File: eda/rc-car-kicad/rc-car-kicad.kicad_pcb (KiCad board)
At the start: 2 copper layers, 81.5 x 40 mm, 55 parts, among them Q1 MMBT3904, Q2 IRLML2246, Q3 IRLML2246, Q4 MMBT3904, Q5 IRLML6244, Q6 IRLML6244, SW1 SW_SPST, U1 TPS3840, U2 MIC3975-5.0YMM, U3 MIC5225-3.3YM5, U4 ATmega164A-A

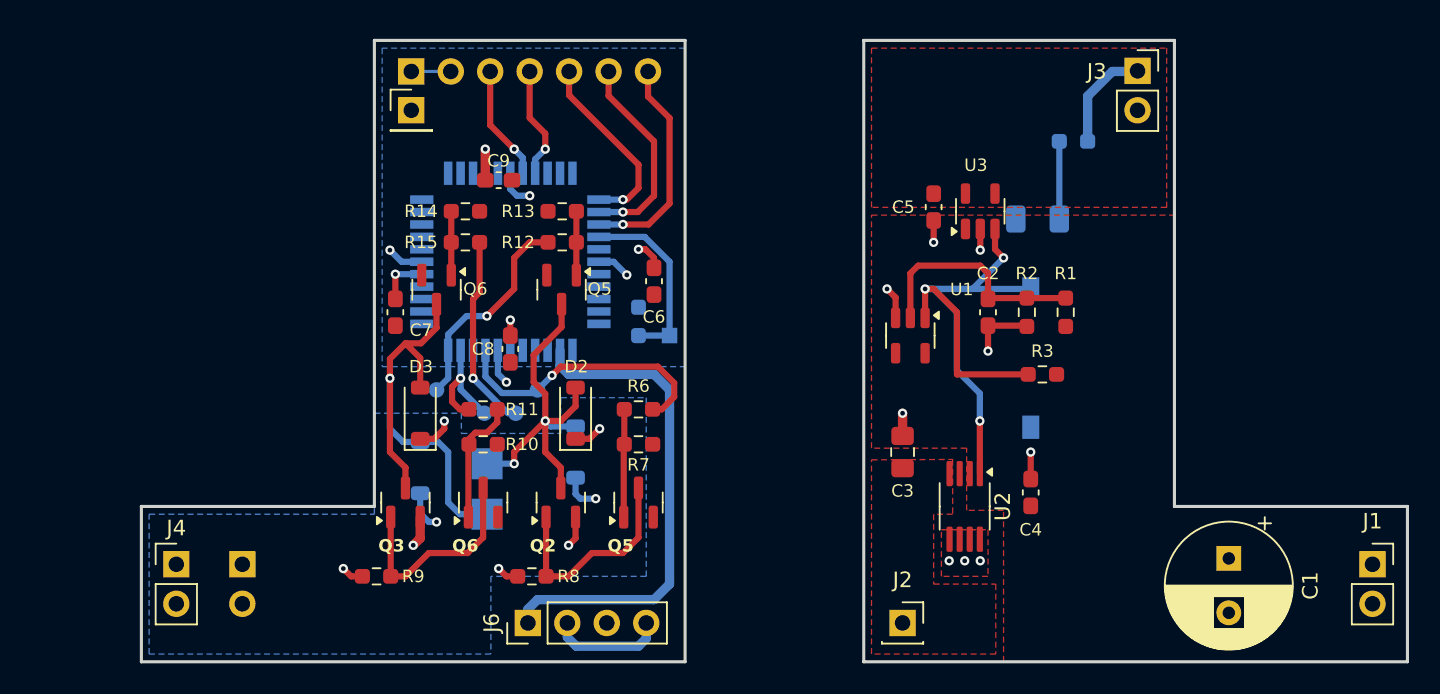
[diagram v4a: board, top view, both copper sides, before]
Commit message: - Modified the header pins a bit on the pcb
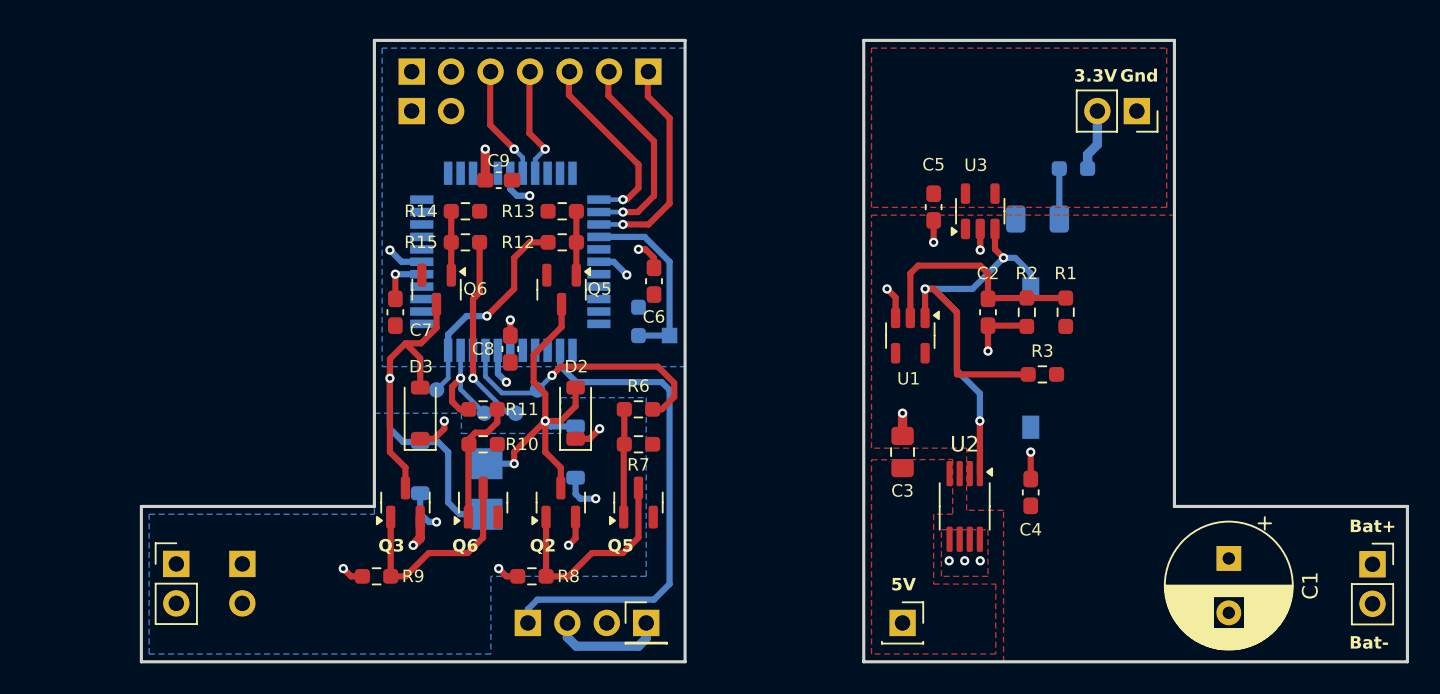
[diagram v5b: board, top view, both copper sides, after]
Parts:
- added J16: ~, _global-libraries:PinHeader_1x02_P2.54mm_Vertical_No_Courtyard, F.Cu at (124.4, 105.0)
- added J17: ~, Connector_PinHeader_2.54mm:PinHeader_1x01_P2.54mm_Vertical, F.Cu at (139.5, 138.0)
- J6: footprint Connector_PinHeader_2.54mm:PinHeader_1x04_P2.54mm_Vertical -> Connector_PinHeader_2.54mm:PinHeader_1x03_P2.54mm_Vertical; moved to B.Cu
- J7: footprint Connector_PinHeader_2.54mm:PinHeader_1x01_P2.54mm_Vertical -> _global-libraries:PinHeader_1x02_P2.54mm_Vertical_No_Courtyard; moved to B.Cu
- J8: footprint Connector_PinHeader_2.54mm:PinHeader_1x07_P2.54mm_Vertical -> Connector_PinHeader_2.54mm:PinHeader_1x05_P2.54mm_Vertical
- moved J8 15.3 mm to (139.6, 102.5), turned to 90 degrees
- moved J3 2.59 mm to (171.1, 105.0), turned to -90 degrees
- moved J7 2.49 mm to (124.4, 102.5), turned to -90 degrees
- moved R4 1.75 mm to (167.0, 108.8)
- turned J6 to -90 degrees
- renumbered Motor- to J10, Motor+ to J9
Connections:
- J3 pad 1: +3.3V Main -> GND Main
- J3 pad 2: GND Main -> +3.3V Main
- J8 pad 1: +3.3V -> /SCK
- J8 pad 2: +3.3V -> /MISO
- J8 pad 3: /CE -> /MOSI
- J8 pad 5: /MOSI -> /CE
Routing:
- net /U1-Reset: track 41.6 -> 37.9 mm
- net +3.3V Main: track 6.78 -> 3.96 mm
- net +3.3V: track 10.7 -> 8.15 mm
- net Net-(D1-A): track 5.00 -> 3.25 mm
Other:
- board text added: "5V"
- board text added: "Bat+"
- board text added: "Bat-"
- board text added: "V+"
- board text added: "V-"

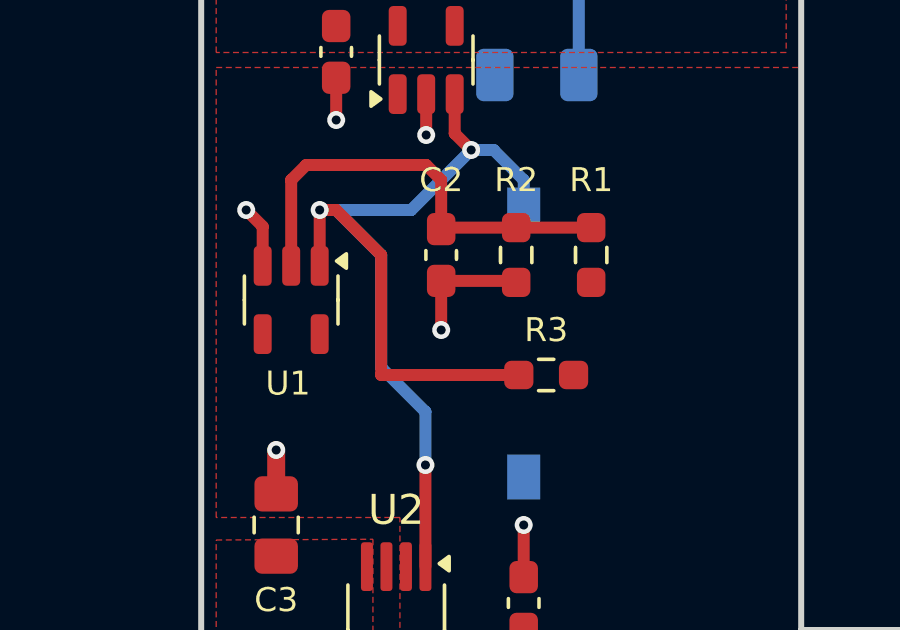
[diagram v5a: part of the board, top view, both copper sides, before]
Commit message: - Updated panelized board. Fixed all design route errors
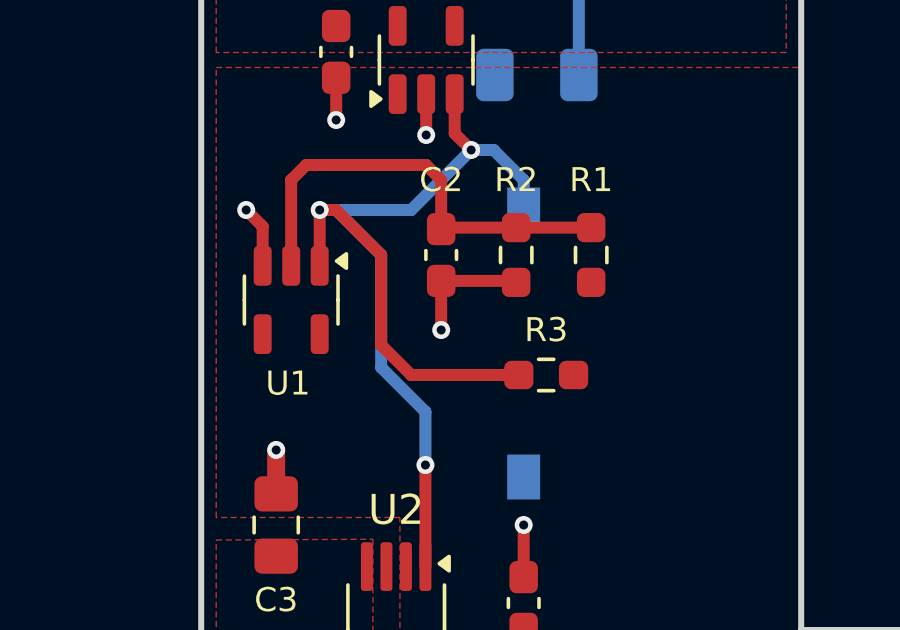
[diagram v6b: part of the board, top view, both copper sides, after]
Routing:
- net /U1-Reset: track 37.9 -> 37.3 mm
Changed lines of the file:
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@@
 	)
 	(setup
+		(stackup
+			(layer "F.SilkS"
+				(type "Top Silk Screen")
+			)
+			(layer "F.Paste"
+				(type "Top Solder Paste")
+			)
+			(layer "F.Mask"
+				(type "Top Solder Mask")
+				(color "Black")
+				(thickness 0.01)
+			)
+			(layer "F.Cu"
+				(type "copper")
+				(thickness 0.035)
+			)
+			(layer "dielectric 1"
+				(type "core")
+				(thickness 1.51)
+				(material "FR4")
+				(epsilon_r 4.5)
+				(loss_tangent 0.02)
+			)
+			(layer "B.Cu"
+				(type "copper")
+				(thickness 0.035)
+			)
+			(layer "B.Mask"
+				(type "Bottom Solder Mask")
+				(color "Black")
+				(thickness 0.01)
+			)
+			(layer "B.Paste"
+				(type "Bottom Solder Paste")
+			)
+			(layer "B.SilkS"
+				(type "Bottom Silk Screen")
+			)
+			(copper_finish "None")
+			(dielectric_constraints no)
+		)
 		(pad_to_mask_clearance 0)
 		(allow_soldermask_bridges_in_footprints no)
@@
 		(tags "Through hole pin header THT 1x02 2.54mm single row")
 		(property "Reference" "J16"
-			(at 0 -2.33 270)
+			(at 0 -2.33 -90)
 			(layer "F.SilkS")
 			(hide yes)
@@
 		)
 		(property "Value" "~"
-			(at 0 4.87 270)
+			(at 0 4.87 -90)
 			(layer "F.Fab")
 			(hide yes)
@@
 		)
 		(fp_text user "${REFERENCE}"
-			(at 0 1.27 360)
+			(at 0 1.27 0)
 			(layer "F.Fab")
 			(effects
@@
 		(tags "Through hole pin header THT 1x05 2.54mm single row")
 		(property "Reference" "J8"
-			(at 0 2.33 270)
+			(at 0 2.33 -90)
 			(layer "B.SilkS")
 			(hide yes)
@@
 		)
 		(property "Value" "~"
-			(at 0 -12.49 270)
+			(at 0 -12.49 -90)
 			(layer "B.Fab")
 			(hide yes)
@@
 		)
 		(fp_text user "${REFERENCE}"
-			(at 0 -5.08 360)
+			(at 0 -5.08 0)
 			(layer "B.Fab")
 			(effects
@@
 	)
 	(segment
-		(start 164.0875 122)
-		(end 159.5 122)
+		(start 160.5 122)
+		(end 159.5 121)
 		(width 0.4)
 		(layer "F.Cu")
@@
 	)
 	(segment
-		(start 159.5 118)
-		(end 158 116.5)
+		(start 161.95 113.95)
+		(end 162.5 114.5)
 		(width 0.4)
 		(layer "F.Cu")
@@
 	)
 	(segment
-		(start 161.95 113.95)
-		(end 162.5 114.5)
+		(start 159.5 121)
+		(end 159.5 118)
 		(width 0.4)
 		(layer "F.Cu")
@@
 	)
 	(segment
-		(start 157.45 116.5)
-		(end 157.45 118.3625)
+		(start 164.0875 122)
+		(end 160.5 122)
 		(width 0.4)
 		(layer "F.Cu")
@@
 	)
 	(segment
-		(start 159.5 122)
-		(end 159.5 118)
+		(start 157.45 116.5)
+		(end 157.45 118.3625)
 		(width 0.4)
 		(layer "F.Cu")
@@
 		(net 30)
 	)
+	(segment
+		(start 159.5 118)
+		(end 158 116.5)
+		(width 0.4)
+		(layer "F.Cu")
+		(net 30)
+	)
 	(via
 		(at 160.975 125)
@@
 		(polygon
 			(pts
-				(xy 154 111.25) (xy 154 107.5) (xy 154 107.5) (xy 154 101) (xy 173 101) (xy 173 111.25)
+				(xy 154 111.25) (xy 154 107.5) (xy 154 101) (xy 173 101) (xy 173 111.25)
 			)
 		)

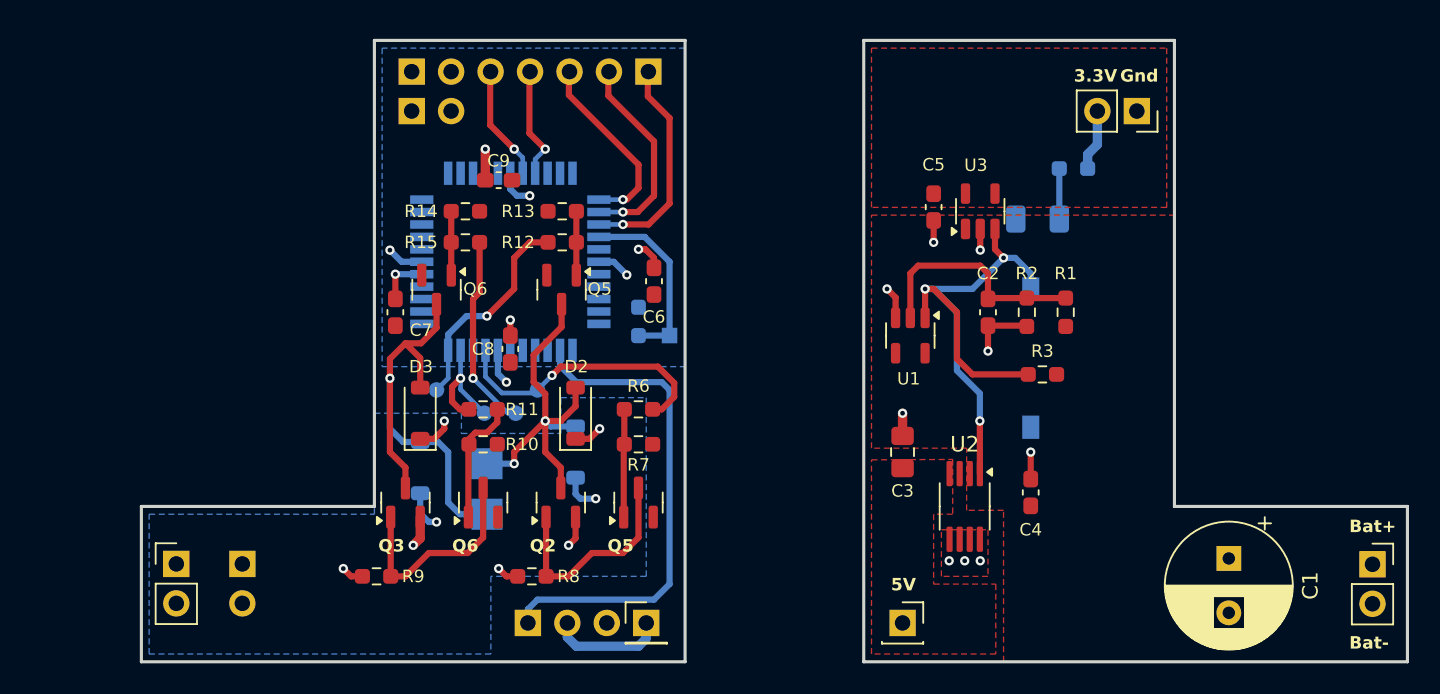
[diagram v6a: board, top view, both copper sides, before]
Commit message: - Documented the schematic and created a pdf of the schematic
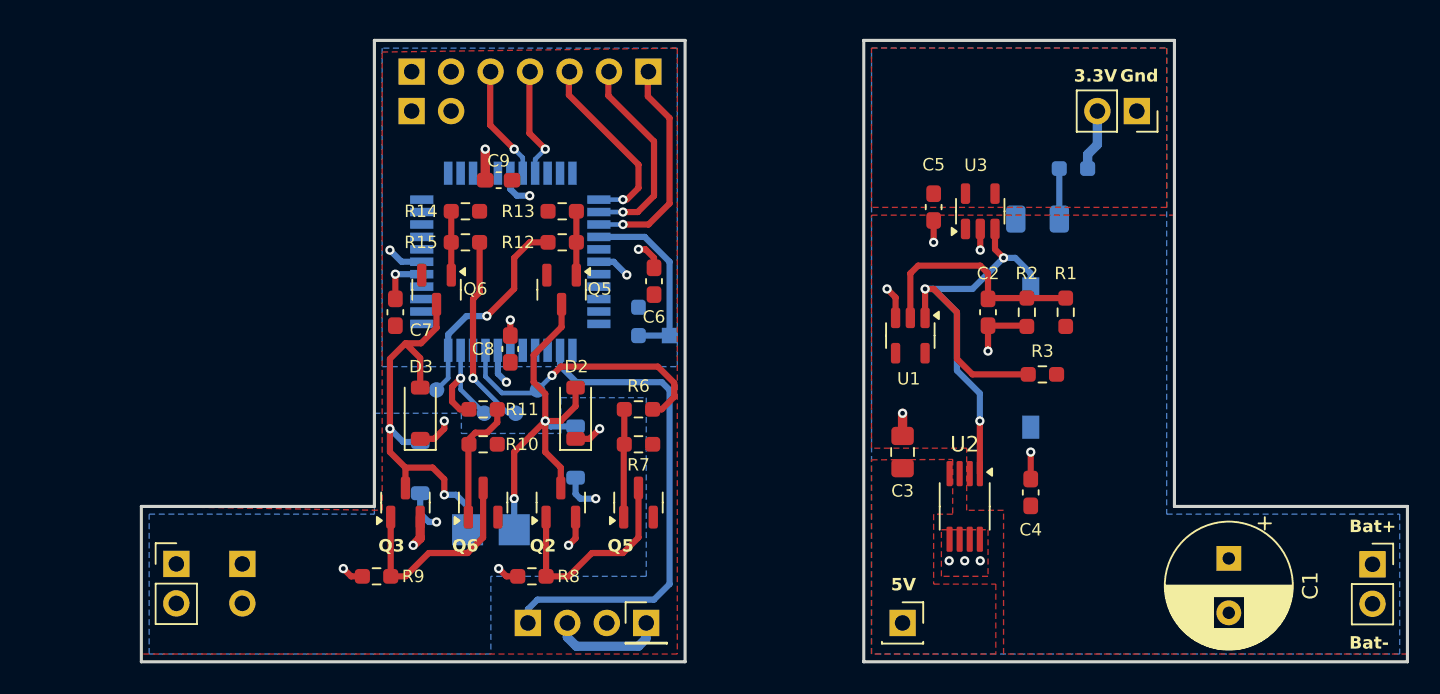
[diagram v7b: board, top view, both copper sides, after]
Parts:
- moved J9 4.60 mm to (131.0, 132.0)
- moved J10 1.60 mm to (128.0, 132.0)
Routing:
- net Net-(D3-A): track 31.0 -> 26.7 mm, vias 1 -> 2
- net Net-(D2-A): track 24.3 -> 26.8 mm
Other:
- board text added: "M+"
- board text added: "M-"
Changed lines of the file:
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@@
 	(footprint "TestPoint:TestPoint_Pad_2.0x2.0mm"
 		(layer "B.Cu")
-		(at 129.25 131 180)
+		(at 128 132 180)
 		(descr "SMD rectangular pad as test Point, square 2.0mm side length")
 		(tags "test point SMD pad rectangle square")
@@
 			(at 0 -2 0)
 			(layer "B.SilkS")
+			(hide yes)
 			(effects
 				(font
@@
 	(footprint "TestPoint:TestPoint_Pad_2.0x2.0mm"
 		(layer "B.Cu")
-		(at 129.25 127.75 180)
+		(at 131 132 180)
 		(descr "SMD rectangular pad as test Point, square 2.0mm side length")
 		(tags "test point SMD pad rectangle square")
@@
 			(at 0 1.85 0)
 			(layer "B.SilkS")
+			(hide yes)
 			(effects
 				(font
@@
 		)
 	)
+	(gr_text "M-"
+		(at 128.75 134.35 0)
+		(layer "B.SilkS")
+		(effects
+			(font
+				(size 0.8 0.8)
+				(thickness 0.2)
+				(bold yes)
+			)
+			(justify left bottom mirror)
+		)
+	)
 	(gr_text "Bat-"
 		(at 114.75 139.75 0)
@@
 		)
 	)
+	(gr_text "M+\n"
+		(at 132.5 134.35 0)
+		(layer "B.SilkS")
+		(effects
+			(font
+				(size 0.8 0.8)
+				(thickness 0.2)
+				(bold yes)
+			)
+			(justify left bottom mirror)
+		)
+	)
 	(gr_text "U1"
 		(at 155.6425 122.75 -0)
@@
 	)
 	(segment
-		(start 133 125)
+		(start 131 130)
 		(end 131 127)
 		(width 0.4)
@@
 	(segment
 		(start 131 127)
-		(end 131 127.75)
+		(end 133 125)
 		(width 0.4)
 		(layer "F.Cu")
@@
 	)
 	(via
-		(at 131 127.75)
+		(at 131 130)
 		(size 0.6)
 		(drill 0.3)
@@
 	)
 	(segment
-		(start 134.95 125.35)
-		(end 133.35 125.35)
+		(start 131 130)
+		(end 131 132)
 		(width 0.4)
 		(layer "B.Cu")
@@
 	)
 	(segment
-		(start 131 127.75)
-		(end 129.25 127.75)
+		(start 134.95 125.35)
+		(end 133.35 125.35)
 		(width 0.4)
 		(layer "B.Cu")
@@
 	)
 	(segment
+		(start 126.5 129.75)
+		(end 126.5 128.75)
+		(width 0.4)
+		(layer "F.Cu")
+		(net 5)
+	)
+	(segment
+		(start 126.5 128.75)
+		(end 125.75 128)
+		(width 0.4)
+		(layer "F.Cu")
+		(net 5)
+	)
+	(segment
 		(start 124 120)
 		(end 123 121)
@@
 	)
 	(segment
+		(start 125.75 128)
+		(end 124 128)
+		(width 0.4)
+		(layer "F.Cu")
+		(net 5)
+	)
+	(segment
 		(start 123 127)
 		(end 124 128)
@@
 	)
 	(via
-		(at 123 122.25)
+		(at 126.5 129.75)
 		(size 0.6)
 		(drill 0.3)
@@
 		(net 5)
 	)
-	(segment
-		(start 127.5 131)
-		(end 129.25 131)
-		(width 0.4)
-		(layer "B.Cu")
-		(net 5)
-	)
-	(segment
-		(start 126.75 127)
-		(end 126.75 130.25)
-		(width 0.4)
-		(layer "B.Cu")
-		(net 5)
-	)
-	(segment
-		(start 124.95 126.35)
-		(end 126.1 126.35)
-		(width 0.4)
-		(layer "B.Cu")
+	(via
+		(at 123 125.5)
+		(size 0.6)
+		(drill 0.3)
+		(layers "F.Cu" "B.Cu")
 		(net 5)
 	)
 	(segment
 		(start 123 125.5)
-		(end 123 122.25)
+		(end 123.85 126.35)
 		(width 0.4)
 		(layer "B.Cu")
@@
 	)
 	(segment
-		(start 124.95 126.35)
-		(end 123.85 126.35)
+		(start 123.85 126.35)
+		(end 124.95 126.35)
 		(width 0.4)
 		(layer "B.Cu")
@@
 	)
 	(segment
-		(start 123.85 126.35)
-		(end 123 125.5)
+		(start 127.25 129.75)
+		(end 126.5 129.75)
 		(width 0.4)
 		(layer "B.Cu")
@@
 	)
 	(segment
-		(start 126.1 126.35)
-		(end 126.75 127)
+		(start 128 130.5)
+		(end 127.25 129.75)
 		(width 0.4)
 		(layer "B.Cu")
@@
 	)
 	(segment
-		(start 126.75 130.25)
-		(end 127.5 131)
+		(start 128 132)
+		(end 128 130.5)
 		(width 0.4)
 		(layer "B.Cu")
@@
 		(polygon
 			(pts
-				(xy 188.5 130.5) (xy 188.5 140.5) (xy 162.5 140.5) (xy 162.5 130.75) (xy 160.125 130.75) (xy 160.125 126.75)
+				(xy 188.5 130.5) (xy 188.5 140) (xy 162.5 140) (xy 162.5 130.75) (xy 160.125 130.75) (xy 160.125 126.75)
 				(xy 154 126.75) (xy 154 111.75) (xy 173.5 111.75) (xy 173.5 130.5)
 			)
@@
 		(polygon
 			(pts
-				(xy 107 140.5) (xy 107 130.5) (xy 122 130.5) (xy 122 100.5) (xy 142 100.5) (xy 142 140.5)
+				(xy 107 140) (xy 107 130.5) (xy 122.5 130.75) (xy 122.5 101.25) (xy 141.5 101) (xy 141.5 140)
 			)
 		)
@@
 		(polygon
 			(pts
-				(xy 153.5 100.5) (xy 173.5 100.5) (xy 173.5 130.5) (xy 188.5 130.5) (xy 188.5 140.5) (xy 153.5 140.5)
+				(xy 154 101) (xy 173 101) (xy 173 131) (xy 188 131) (xy 188 140) (xy 154 140)
 			)
 		)
@@
 		(polygon
 			(pts
-				(xy 122.5 101) (xy 122.5 121.5) (xy 142 121.5) (xy 142 101)
+				(xy 122.5 101) (xy 122.5 121.5) (xy 141.5 121.5) (xy 141.5 101)
 			)
 		)

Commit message: - Added an images directory with images of the pcb and the schematic - Added a revision number to the pcb. - Finalized pcb and schematic
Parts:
- C1: footprint Capacitor_THT:CP_Radial_D8.0mm_P3.50mm -> Capacitor_THT:CP_Radial_D6.3mm_P2.50mm
- moved C1 0.47 mm to (177.0, 134.3)
- renumbered J9 to M+1, J10 to M-1
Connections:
- net +8.2V renamed +8.4V
- net +8.2V Main renamed +8.4V Main
